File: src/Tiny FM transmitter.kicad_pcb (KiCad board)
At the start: 2 copper layers, 25.4 x 25.4 mm, 14 parts, among them U1 MAX2605/6/7/8/9, U2 AP2204K-2.8

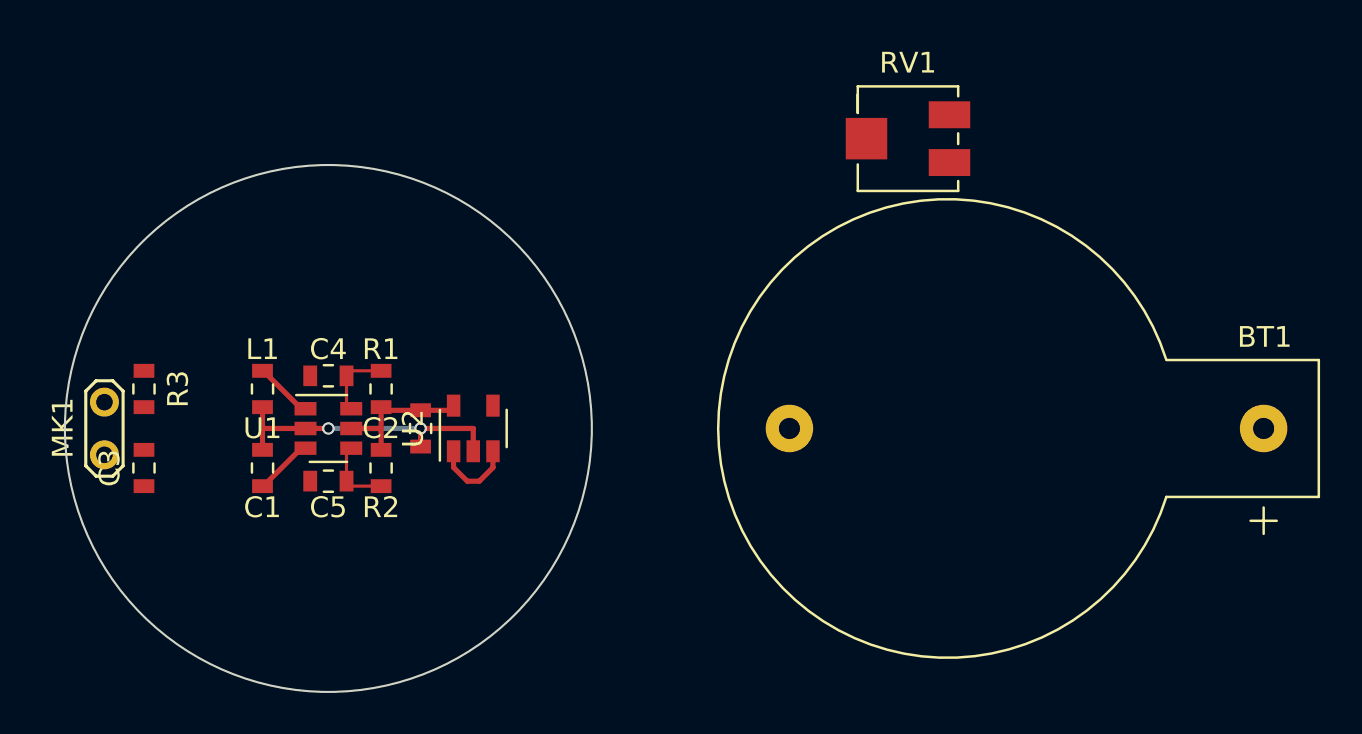
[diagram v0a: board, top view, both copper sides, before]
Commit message: finished routing. successfull DRC
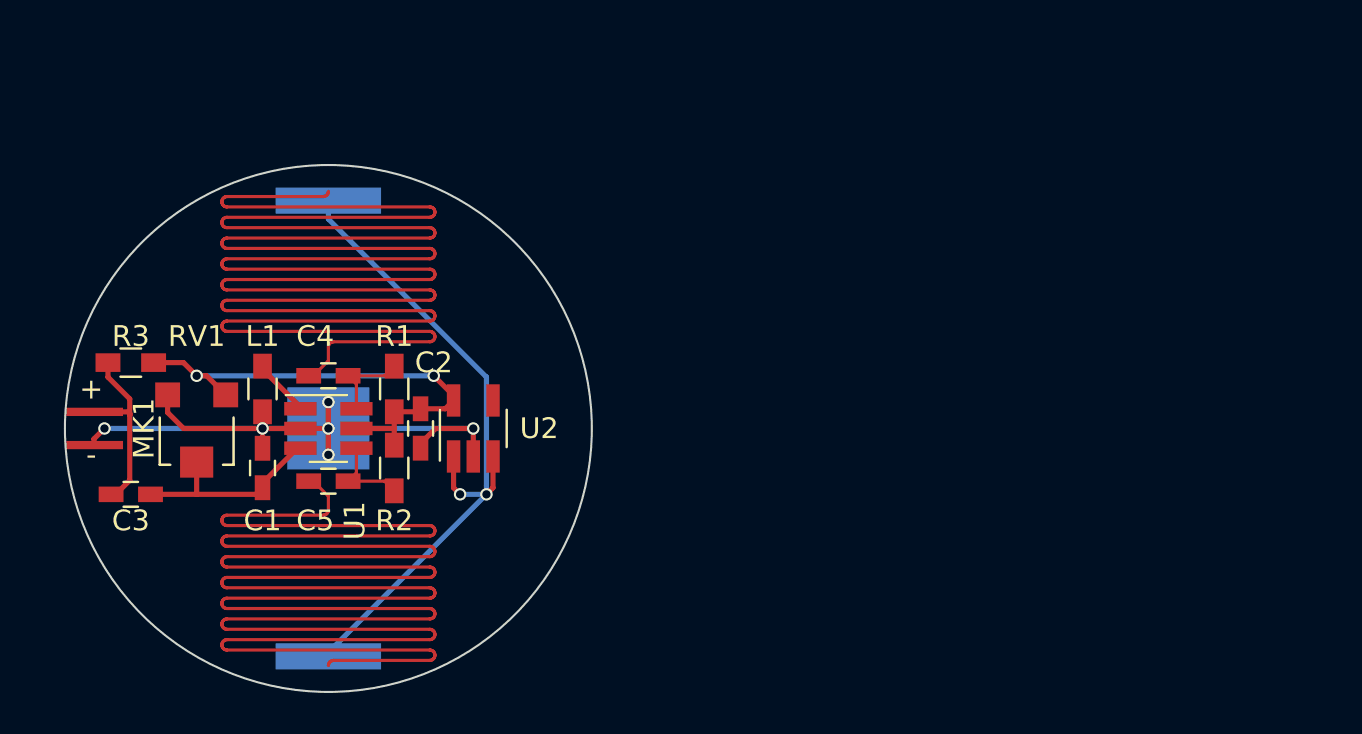
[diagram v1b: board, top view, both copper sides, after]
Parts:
- BT1: footprint Battery:BatteryHolder_CR2032H -> Battery_Holders:Keystone_3034_1x20mm-CoinCell; moved to B.Cu
- C1, C2, C3, C4, C5: footprint Capacitor_SMD:C_0603_1608Metric -> Capacitors_SMD:C_0603_HandSoldering
- L1: footprint Inductor_SMD:L_0603_1608Metric -> Inductors_SMD:L_0603_HandSoldering
- MK1: footprint TestPoint:TestPoint_2Pads_Pitch2.54mm_Drill0.8mm -> Tiny FM transmitter:HM4522P-423-G
- R1, R2, R3: footprint Resistor_SMD:R_0603_1608Metric -> Resistors_SMD:R_0603_HandSoldering
- RV1: footprint Potentiometer_SMD:Potentiometer_Bourns_3224J_Horizontal -> Potentiometers:Potentiometer_Trimmer-EVM3E
- U1: footprint Package_TO_SOT_SMD:SOT-23-6 -> TO_SOT_Packages_SMD:SOT-23-6_Handsoldering
- U2: footprint Package_TO_SOT_SMD:SOT-23-5 -> TO_SOT_Packages_SMD:SOT-23-5_HandSoldering
- moved BT1 45.1 mm to (184.2, 101.6), turned to 270 degrees
- moved RV1 37.0 mm to (177.8, 101.6), turned to 180 degrees
- moved MK1 2.29 mm to (171.4, 101.6), turned to 0 degrees
- moved C3 1.42 mm to (174.6, 104.8), turned to 180 degrees
- moved R3 1.42 mm to (174.6, 98.4), turned to 180 degrees
- moved R1 0.63 mm to (187.3, 99.7)
- moved R2 0.63 mm to (187.3, 103.5)
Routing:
- net /ANT+: track 0.00 -> 150.0 mm
- net /ANT-: track 0.00 -> 150.0 mm
- net /+BAT: track 4.01 -> 33.5 mm, vias 0 -> 2
- net GND: track 14.2 -> 36.4 mm, vias 2 -> 6
- net VCC: track 7.15 -> 23.7 mm, vias 0 -> 2
- net Net-(C3-Pad2): track 0.00 -> 9.14 mm
- net Net-(C1-Pad1): track 2.83 -> 9.83 mm
- net /OUT-: track 3.65 -> 4.17 mm
- net /OUT+: track 3.65 -> 4.17 mm

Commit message: BOM
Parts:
- removed the C1 at (181.0, 103.5)
- added C3: 1nF, Capacitors_SMD:C_0603_HandSoldering, F.Cu at (181.0, 103.5)
- RV1: value POT -> 10k
- U1: value MAX2605/6/7/8/9 -> MAX2606
- renumbered C2 to C1, C3 to C2
